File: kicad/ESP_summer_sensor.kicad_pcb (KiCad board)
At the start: 2 copper layers, 59.1 x 42.5 mm, 19 parts, among them J1 JACK2.1MM, J3 TERM-1X02-FABLAB, J4 Conn_01x04, J5 Conn_01x04, J6 Conn_01x06, M1 SPDTSWITCH, U2 MIC39100-3.3_SOT223, U3 ESP-12E

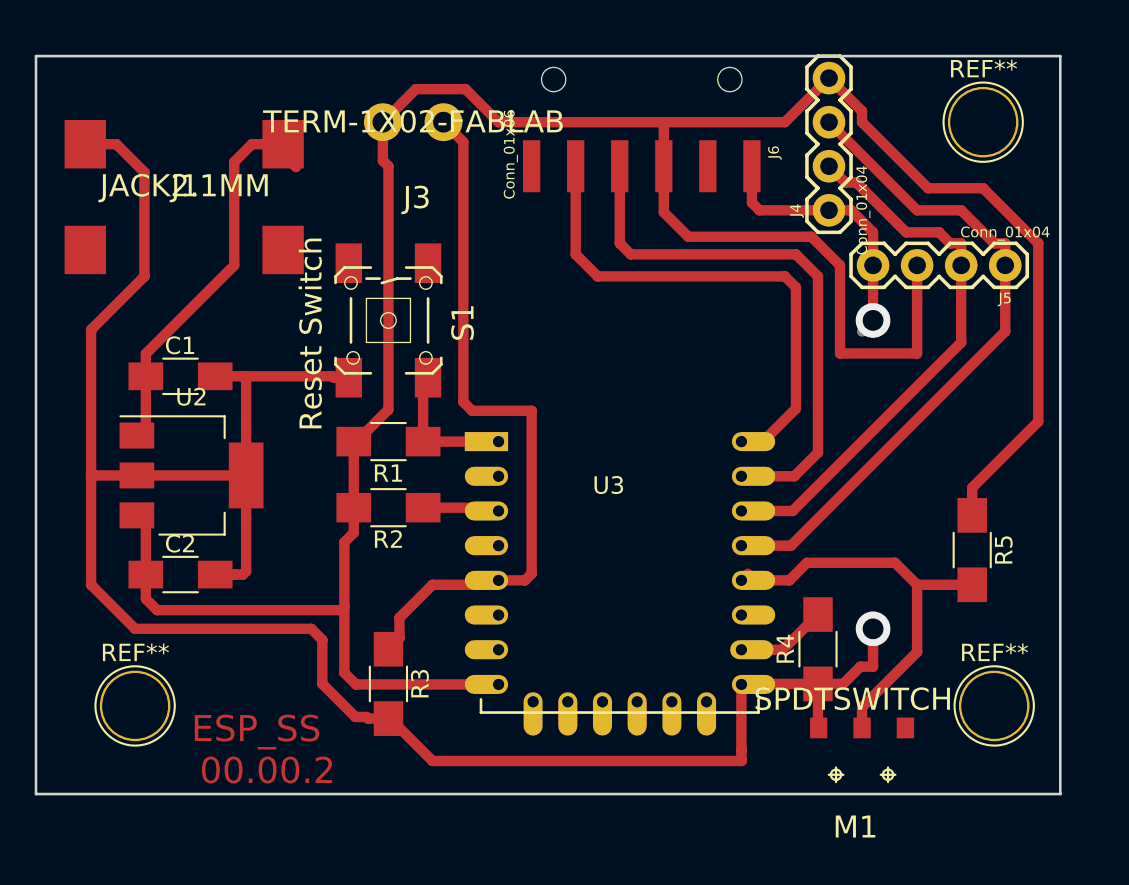
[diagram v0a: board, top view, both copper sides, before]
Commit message: Update: PCB version 00.00.3 Fixed layout and footprint issues
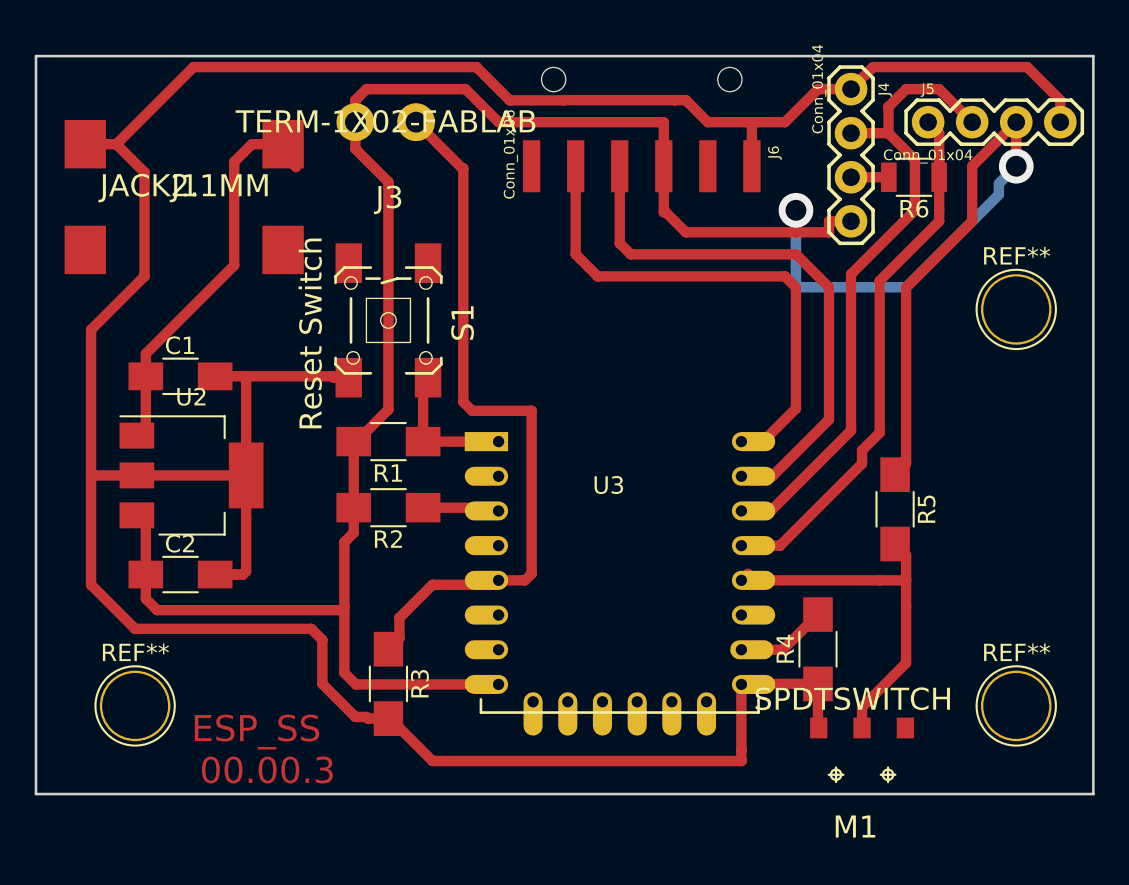
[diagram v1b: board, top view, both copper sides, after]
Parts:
- added R6: 0, Resistors_SMD:R_1206, F.Cu at (167.5, 87.6)
- moved REF** 11.0 mm to (173.4, 95.2)
- moved J5 9.38 mm to (168.3, 84.5), turned to 0 degrees
- moved J4 7.10 mm to (163.8, 82.5), turned to 270 degrees
- moved R5 5.03 mm to (166.4, 106.8)
- moved J3 1.58 mm to (137.1, 84.5)
- moved REF** 1.27 mm to (173.4, 118.1)
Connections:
- J1 pad SHUN: (no net) -> Net-(J1-PadSHUN)
- J6 pad 2: (no net) -> /CTS
- J6 pad 6: (no net) -> /DTR
- M1 pad 3: (no net) -> Net-(M1-Pad3)
- S1 pad 1: (no net) -> Net-(S1-Pad1)
- S1 pad 3: (no net) -> Net-(S1-Pad3)
- U3 pad 11: (no net) -> Net-(U3-Pad11)
- U3 pad 17: (no net) -> Net-(U3-Pad17)
- U3 pad 18: (no net) -> Net-(U3-Pad18)
- U3 pad 19: (no net) -> Net-(U3-Pad19)
- U3 pad 2: (no net) -> Net-(U3-Pad2)
- U3 pad 20: (no net) -> Net-(U3-Pad20)
- U3 pad 21: (no net) -> Net-(U3-Pad21)
- U3 pad 22: (no net) -> Net-(U3-Pad22)
- U3 pad 4: (no net) -> Net-(U3-Pad4)
- U3 pad 6: (no net) -> Net-(U3-Pad6)
- U3 pad 7: (no net) -> Net-(U3-Pad7)
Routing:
- net GND: track 135.9 -> 177.2 mm, vias 2 -> 0
- net +3V3: track 152.8 -> 144.9 mm, vias 0 -> 2
- net /SCL: track 31.9 -> 37.3 mm
- net /SDA: track 38.5 -> 34.1 mm
- net Net-(M1-Pad2): track 24.7 -> 22.3 mm
- net /Pulse: track 40.9 -> 41.6 mm
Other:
- board size 59.1 x 42.5 mm -> 61 x 42.5 mm
- board text added: "ESP_SS 00.00.3"
- board text removed: "ESP_SS 00.00.2"
